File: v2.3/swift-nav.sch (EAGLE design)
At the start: 177 parts, among them J1 SMA_EDGE, J6 ZX62-B-5PA, Q1 IRLML6401, U1 6SLX9FTG256, U10 MAX2769, U12 PT7M8206B33TA5EX, U13 M25PX80, U2 LTC3407A_DFN, U3 STM32-M-64-LQFP, U4 7Q-16.368MBG-T, U5 SMA_PATCH_SMDGND, U6 93LC56BT-I/OT, U7 FT232HQ, U8 B4050, U9 XC2401, X3 FPGA DEBUG, X4 NX5032GA-12M, X5 CONN_5-2

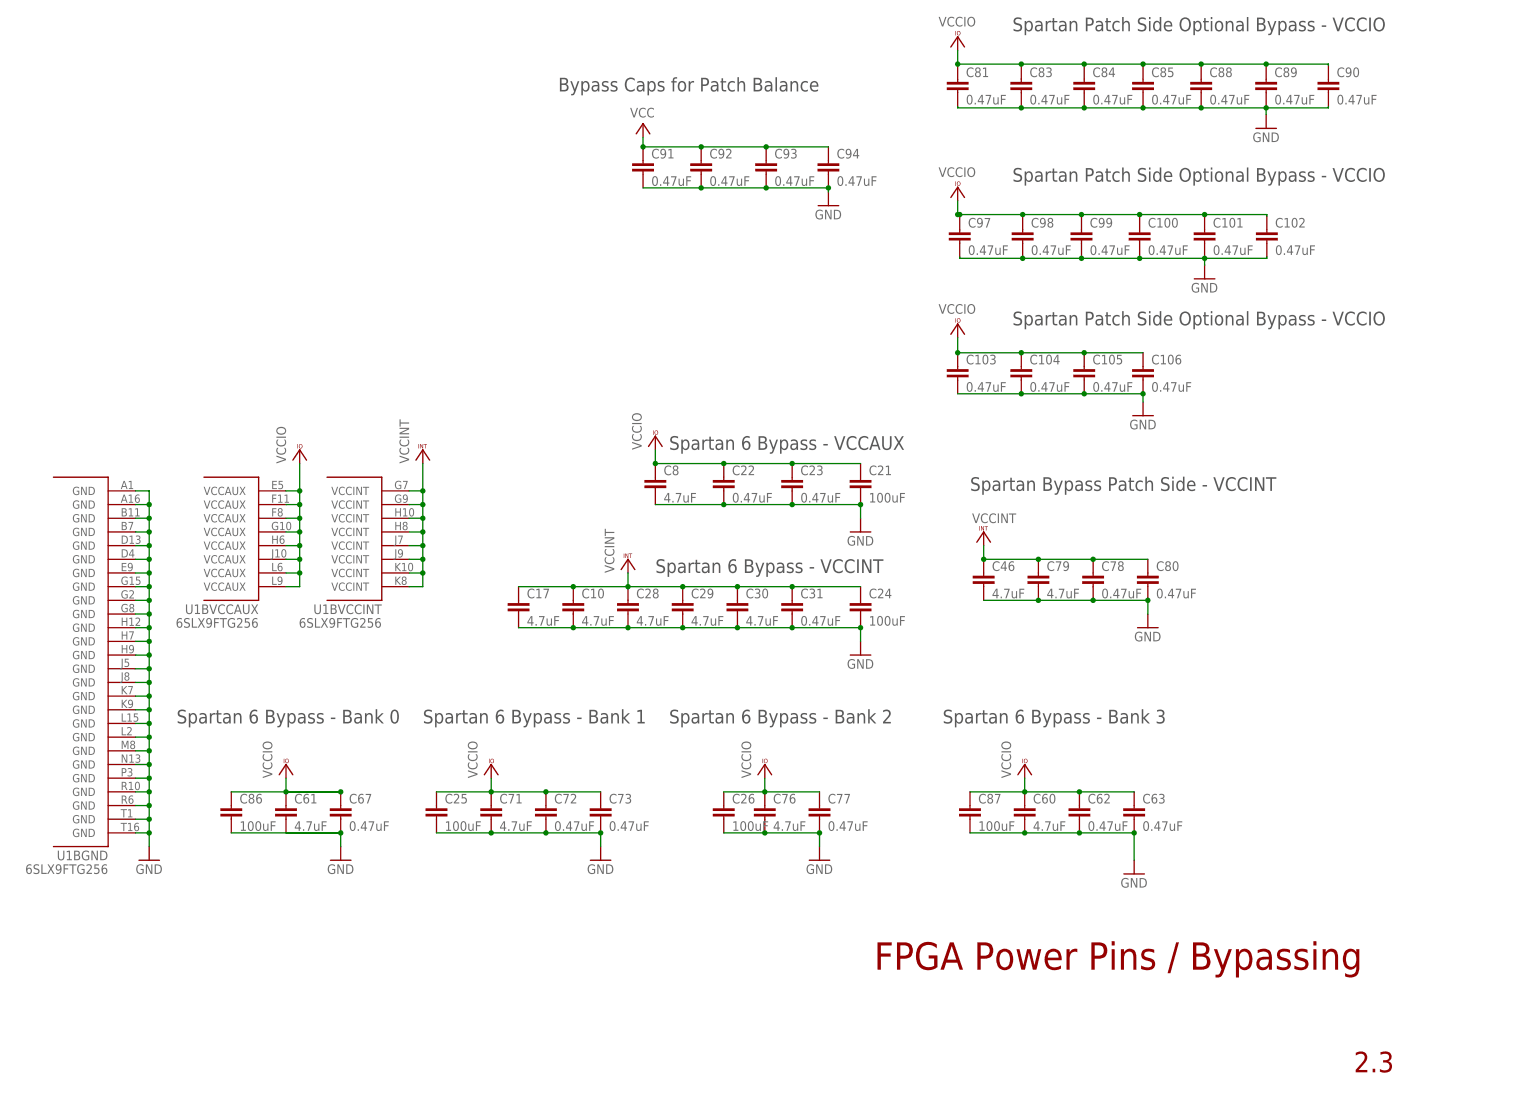
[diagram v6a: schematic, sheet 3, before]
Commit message: Removed capacitors from bottom of board
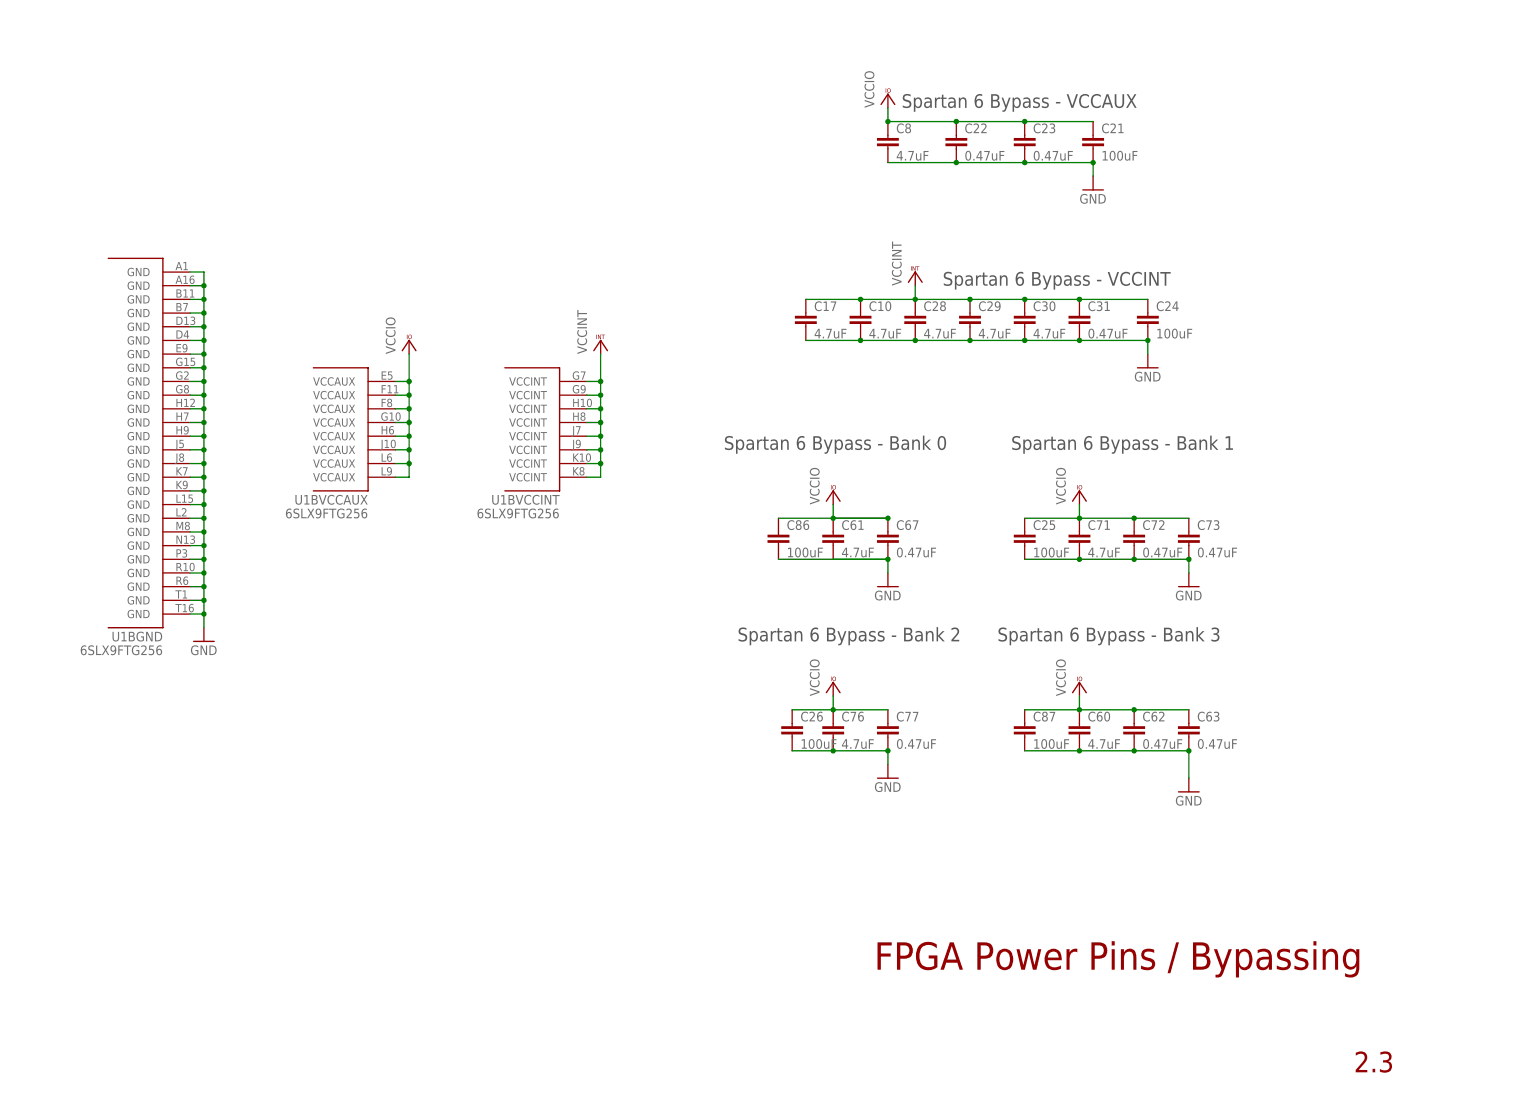
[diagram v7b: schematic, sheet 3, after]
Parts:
- removed C100, C101, C102, C103, C104, C105, C106, C78, C80, C81, C83, C84, C85, C88, C89, C90, C91, C92, C93, C94, C97, C98, C99: 0.47uF, rcl:C-EUC0402
- removed C46, C79: 4.7uF, rcl:C-EUC0603K
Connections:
- net GND: no longer C100.2, C101.2, C102.2, C103.2, C104.2, C105.2, C106.2, C46.2, C78.2, C79.2, C80.2, C81.2, C83.2, C84.2, C85.2, C88.2, C89.2, C90.2, C91.2, C92.2, C93.2, C94.2, C97.2, C98.2, C99.2
- net VCC: no longer C91.1, C92.1, C93.1, C94.1
- net VCCINT: no longer C46.1, C78.1, C79.1, C80.1
- net VCCIO: no longer C100.1, C101.1, C102.1, C103.1, C104.1, C105.1, C106.1, C81.1, C83.1, C84.1, C85.1, C88.1, C89.1, C90.1, C97.1, C98.1, C99.1
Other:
- note removed: "Bypass Caps for Patch Balance"
- note removed: "Spartan Bypass Patch Side - VCCINT"
- note removed: "Spartan Patch Side Optional Bypass - VCCIO"
- moved on the sheet: C10, C17, C21, C22, C23, C24, C25, C26, C28, C29, C30, C31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

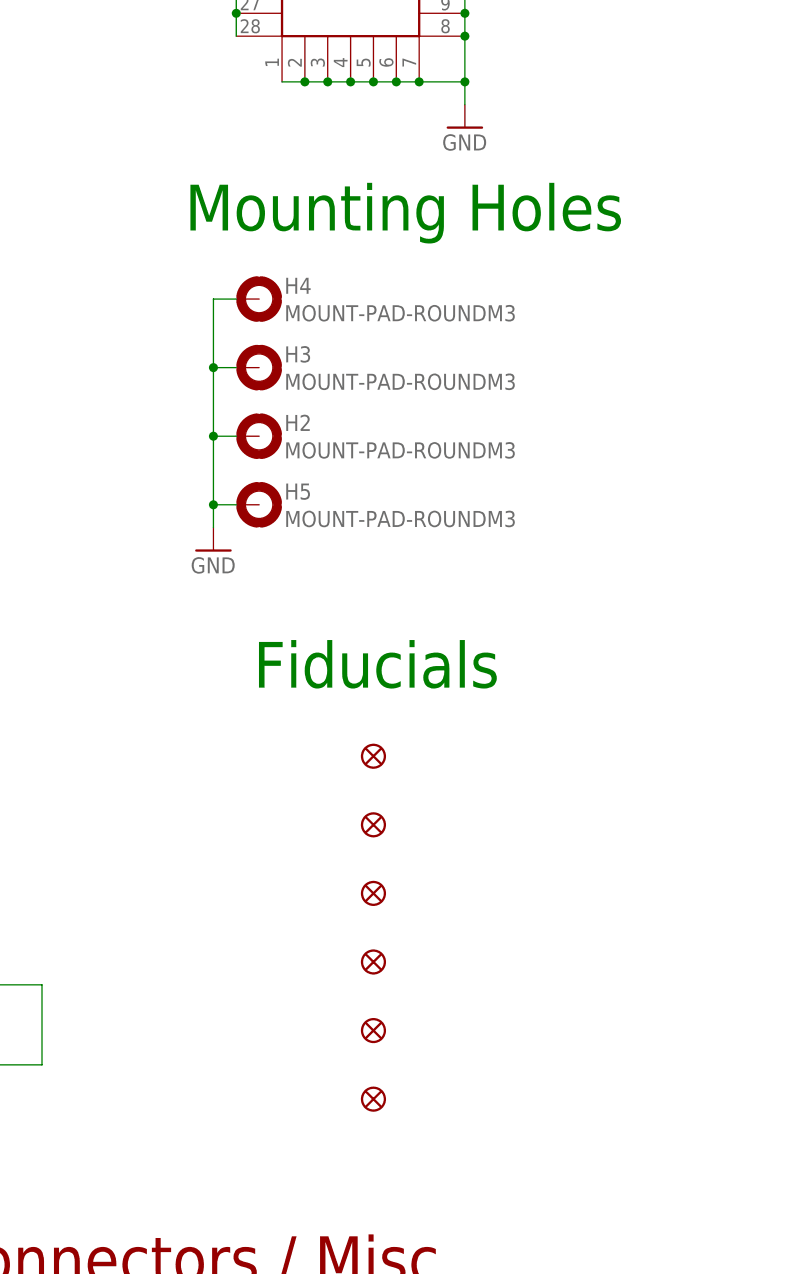
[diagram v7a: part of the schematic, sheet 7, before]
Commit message: Removed fiducials from bottom of board
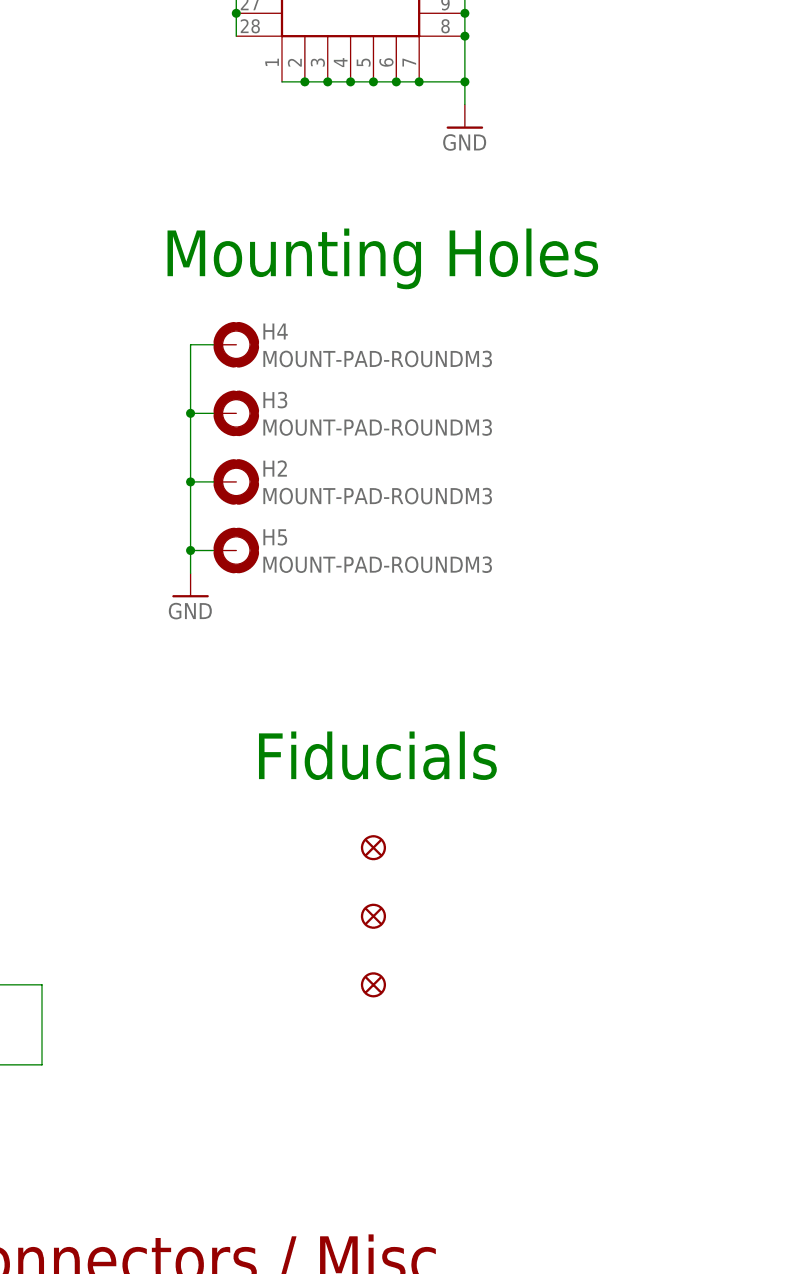
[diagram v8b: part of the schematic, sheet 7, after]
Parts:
- removed JP5, JP6, JP7: FIDUCIAL1.5X3, aspirin:FIDUCIAL1.5X3
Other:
- moved on the sheet: H2, H3, H4, H5
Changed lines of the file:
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@@
 <part name="SHLD2" library="jobygnss" deviceset="BMI-S-208" device=""/>
 <part name="GND4" library="supply1" deviceset="GND" device=""/>
-<part name="JP5" library="aspirin" deviceset="FIDUCIAL" device="1.5X3"/>
-<part name="JP6" library="aspirin" deviceset="FIDUCIAL" device="1.5X3"/>
-<part name="JP7" library="aspirin" deviceset="FIDUCIAL" device="1.5X3"/>
 <part name="JP8" library="aspirin" deviceset="FIDUCIAL" device="1.5X3"/>
 <part name="JP9" library="aspirin" deviceset="FIDUCIAL" device="1.5X3"/>
@@
 <text x="269.24" y="10.16" size="3.81" layer="94" rot="R180">2.3</text>
 <text x="175.26" y="25.4" size="5.08" layer="94">Connectors / Misc</text>
-<text x="202.565" y="142.24" size="5.08" layer="91">Mounting Holes</text>
-<text x="210.185" y="91.44" size="5.08" layer="91">Fiducials</text>
+<text x="200.025" y="137.16" size="5.08" layer="91">Mounting Holes</text>
+<text x="210.185" y="81.28" size="5.08" layer="91">Fiducials</text>
 </plain>
 <instances>
-<instance part="GND8" gate="1" x="205.74" y="106.68"/>
-<instance part="H2" gate="G$1" x="210.82" y="119.38"/>
-<instance part="H3" gate="G$1" x="210.82" y="127"/>
-<instance part="H4" gate="G$1" x="210.82" y="134.62"/>
-<instance part="H5" gate="G$1" x="210.82" y="111.76"/>
+<instance part="GND8" gate="1" x="203.2" y="101.6"/>
+<instance part="H2" gate="G$1" x="208.28" y="114.3"/>
+<instance part="H3" gate="G$1" x="208.28" y="121.92"/>
+<instance part="H4" gate="G$1" x="208.28" y="129.54"/>
+<instance part="H5" gate="G$1" x="208.28" y="106.68"/>
 <instance part="SHLD2" gate="G$1" x="208.28" y="168.91" smashed="yes">
 <attribute name="NAME" x="213.36" y="189.23" size="1.778" layer="95"/>
@@
 </instance>
 <instance part="GND4" gate="1" x="233.68" y="153.67"/>
-<instance part="JP5" gate="G$1" x="223.52" y="83.82"/>
-<instance part="JP6" gate="G$1" x="223.52" y="76.2"/>
-<instance part="JP7" gate="G$1" x="223.52" y="68.58"/>
-<instance part="JP8" gate="G$1" x="223.52" y="60.96"/>
-<instance part="JP9" gate="G$1" x="223.52" y="53.34"/>
-<instance part="JP10" gate="G$1" x="223.52" y="45.72"/>
+<instance part="JP8" gate="G$1" x="223.52" y="73.66"/>
+<instance part="JP9" gate="G$1" x="223.52" y="66.04"/>
+<instance part="JP10" gate="G$1" x="223.52" y="58.42"/>
 <instance part="GND43" gate="1" x="76.2" y="43.18"/>
 <instance part="GND44" gate="1" x="116.84" y="93.98"/>
@@
 <segment>
 <pinref part="GND8" gate="1" pin="GND"/>
-<wire x1="208.28" y1="111.76" x2="205.74" y2="111.76" width="0.1524" layer="91"/>
-<wire x1="205.74" y1="111.76" x2="205.74" y2="109.22" width="0.1524" layer="91"/>
+<wire x1="205.74" y1="106.68" x2="203.2" y2="106.68" width="0.1524" layer="91"/>
+<wire x1="203.2" y1="106.68" x2="203.2" y2="104.14" width="0.1524" layer="91"/>
 <pinref part="H2" gate="G$1" pin="MOUNT"/>
-<wire x1="208.28" y1="119.38" x2="205.74" y2="119.38" width="0.1524" layer="91"/>
-<wire x1="205.74" y1="119.38" x2="205.74" y2="111.76" width="0.1524" layer="91"/>
-<junction x="205.74" y="111.76"/>
+<wire x1="205.74" y1="114.3" x2="203.2" y2="114.3" width="0.1524" layer="91"/>
+<wire x1="203.2" y1="114.3" x2="203.2" y2="106.68" width="0.1524" layer="91"/>
+<junction x="203.2" y="106.68"/>
 <pinref part="H4" gate="G$1" pin="MOUNT"/>
-<wire x1="208.28" y1="134.62" x2="205.74" y2="134.62" width="0.1524" layer="91"/>
-<wire x1="205.74" y1="134.62" x2="205.74" y2="127" width="0.1524" layer="91"/>
-<junction x="205.74" y="119.38"/>
+<wire x1="205.74" y1="129.54" x2="203.2" y2="129.54" width="0.1524" layer="91"/>
+<wire x1="203.2" y1="129.54" x2="203.2" y2="121.92" width="0.1524" layer="91"/>
+<junction x="203.2" y="114.3"/>
 <pinref part="H3" gate="G$1" pin="MOUNT"/>
-<wire x1="205.74" y1="127" x2="205.74" y2="119.38" width="0.1524" layer="91"/>
-<wire x1="208.28" y1="127" x2="205.74" y2="127" width="0.1524" layer="91"/>
-<junction x="205.74" y="127"/>
+<wire x1="203.2" y1="121.92" x2="203.2" y2="114.3" width="0.1524" layer="91"/>
+<wire x1="205.74" y1="121.92" x2="203.2" y2="121.92" width="0.1524" layer="91"/>
+<junction x="203.2" y="121.92"/>
 <pinref part="H5" gate="G$1" pin="MOUNT"/>
 </segment>
